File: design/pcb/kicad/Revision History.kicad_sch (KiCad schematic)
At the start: 0 parts

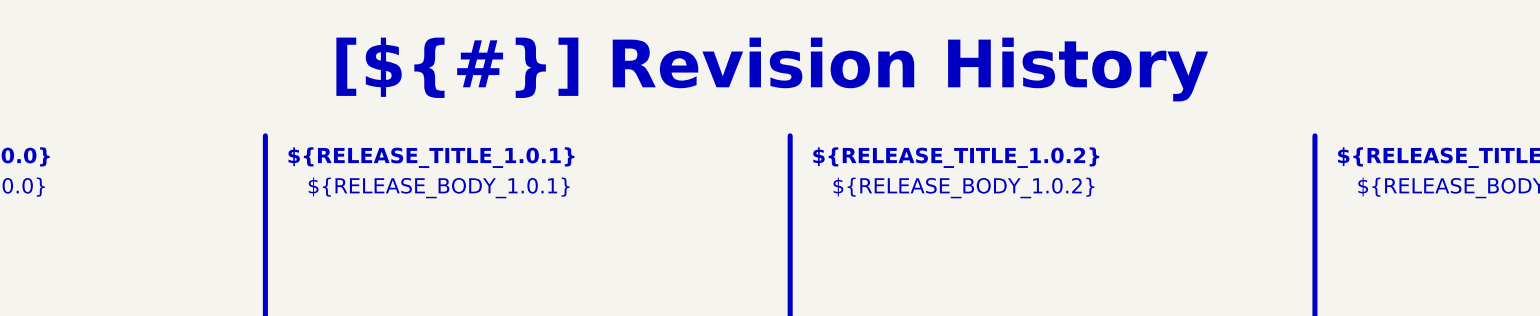
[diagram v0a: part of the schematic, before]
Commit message: Add LCD and STLink schematic sheets, update KiCad project files
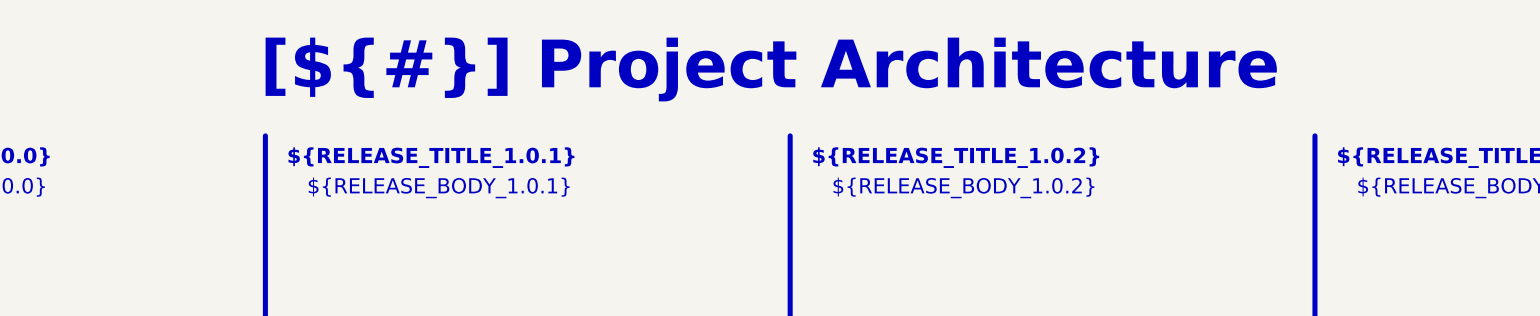
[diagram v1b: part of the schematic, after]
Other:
- title: Revision History -> Project Architecture
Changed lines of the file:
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@@
 	(paper "A4")
 	(title_block
-		(title "Revision History")
+		(title "Project Architecture")
 		(date "2025-01-12")
 		(rev "${REVISION}")
